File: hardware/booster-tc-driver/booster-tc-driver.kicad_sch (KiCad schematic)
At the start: 52 parts, among them J1 62201021121, J2 EHT-105-01-S-D, Q1 T2N7002AK, U1 STM32F405RGTx, U2 LT1963AxST-3.3, U3 MAX9202ESD+, U4 IF-D95T << must be T, U6 IF-D95T << must be T, U7 TC7662Bx0A

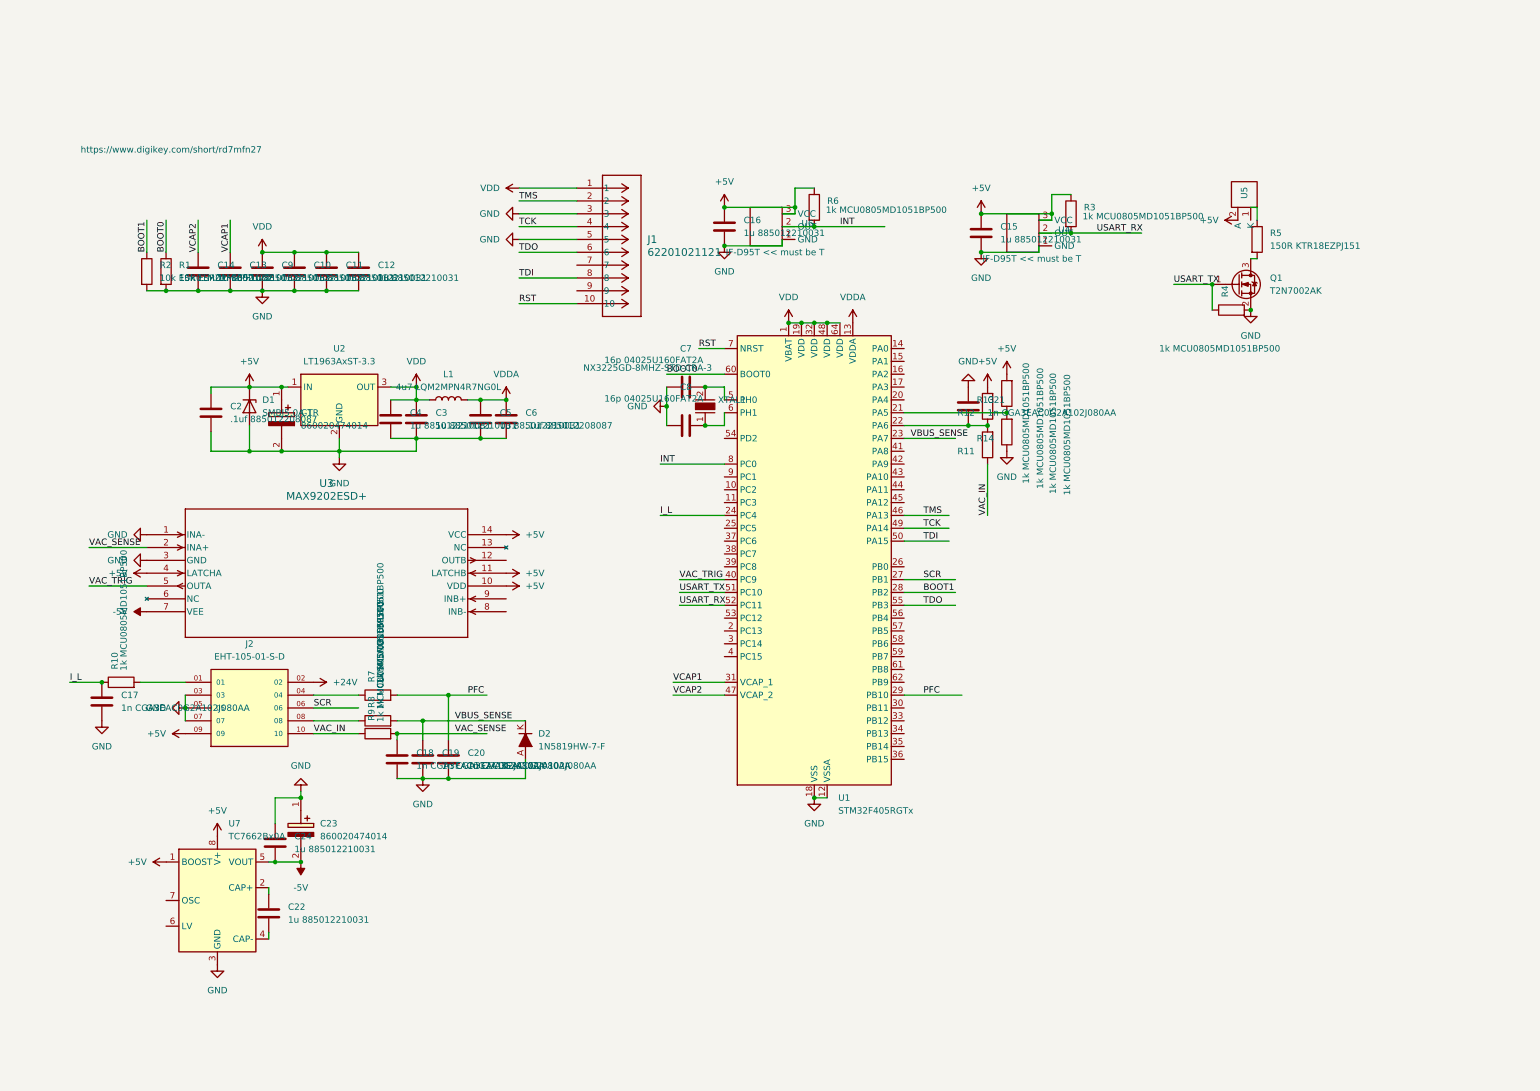
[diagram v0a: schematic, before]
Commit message: pin assignments
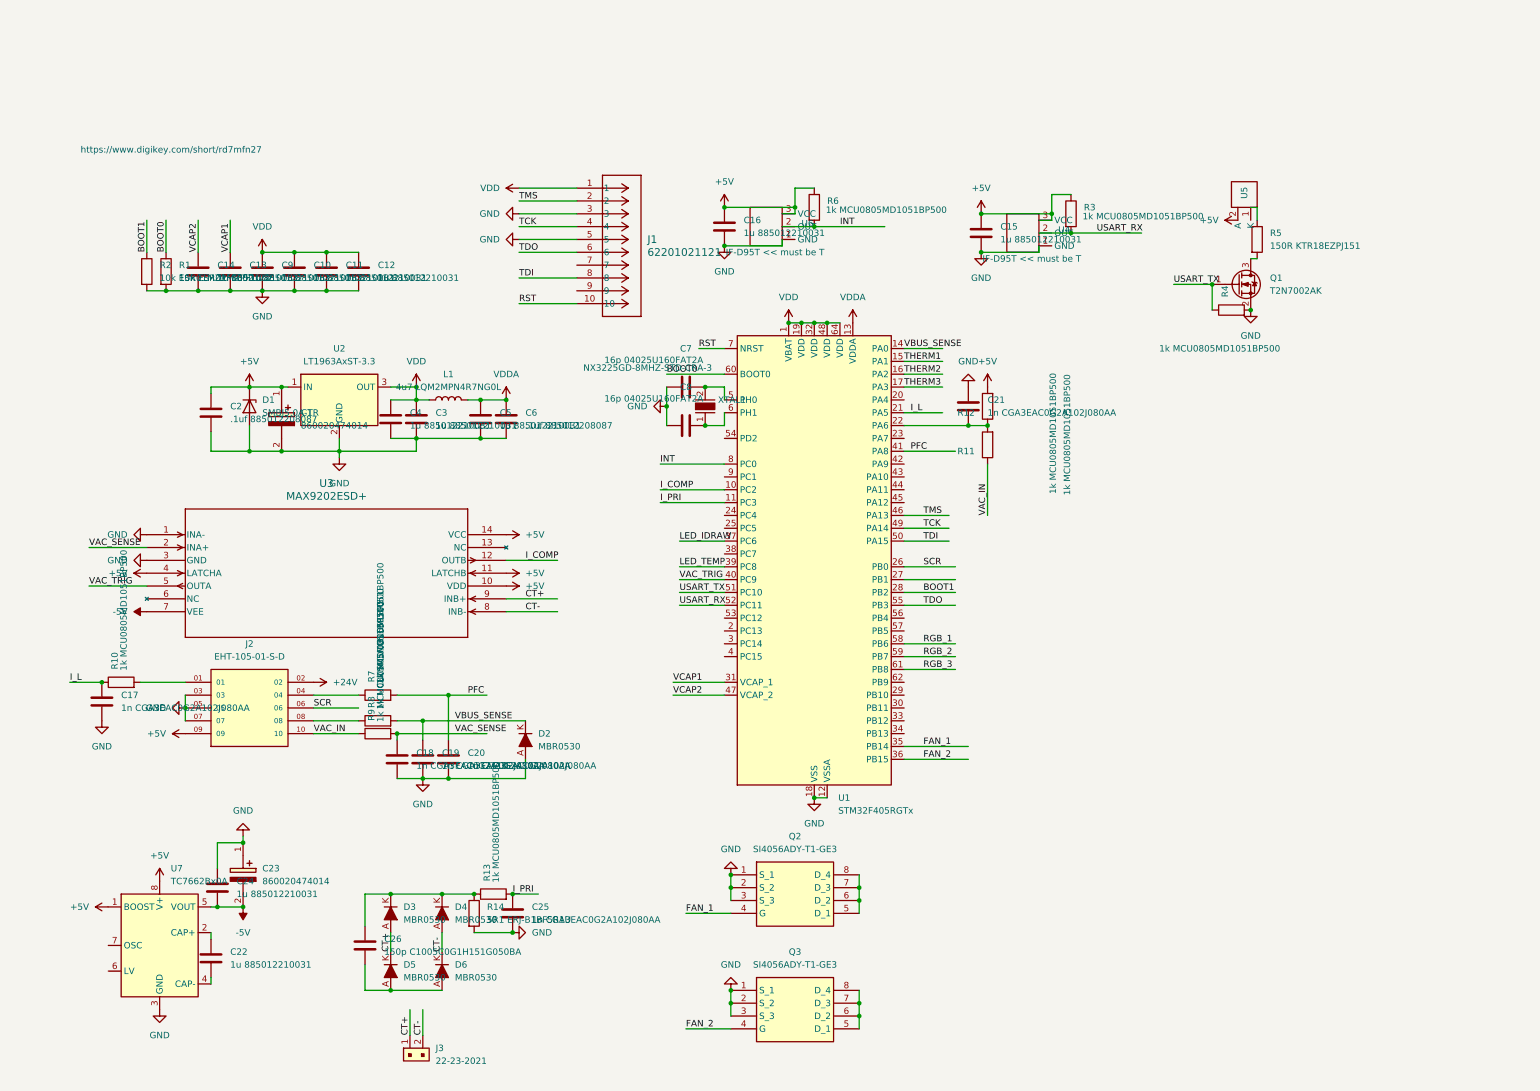
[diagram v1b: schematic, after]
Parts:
- added C25: 1n CGA3EAC0G2A102J080AA, Capacitor_SMD:C_0603_1608Metric_Pad1.08x0.95mm_HandSolder, symbol Device:C
- added C26: 150p C1005C0G1H151G050BA, Capacitor_SMD:C_01005_0402Metric_Pad0.57x0.30mm_HandSolder, symbol Device:C
- added D3, D4, D5, D6: MBR0530, digikey-footprints:SOD-123, symbol dk_Diodes-Rectifiers-Single:1N5819HW-7-F
- added J3: 22-23-2021, digikey-footprints:PinHeader_1x2_P2.54mm_Drill1.02mm, symbol dk_Rectangular-Connectors-Headers-Male-Pins:22-23-2021
- added Q2, Q3: SI4056ADY-T1-GE3, Library:SOIC127P600X175-8N, symbol SI4056ADY-T1-GE3:SI4056ADY-T1-GE3
- D2: value 1N5819HW-7-F -> MBR0530
- R14: value 1k MCU0805MD1051BP500 -> 5R1 ERJ-B1BF5R1U; footprint Resistor_SMD:R_0805_2012Metric_Pad1.20x1.40mm_HandSolder -> Resistor_SMD:R_1020_2550Metric_Pad1.33x5.20mm_HandSolder
- U3: footprint 21-0041B_14 -> Library:21-0041B_14-L
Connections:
- net +5V: no longer R13.2
- net GND: now also R14.2, C25.2, Q2.1 (S_1), Q2.2 (S_2), Q2.3 (S_3), Q3.1 (S_1), Q3.2 (S_2), Q3.3 (S_3); no longer R14.1
- net I_L: now also U1.21 (PA5); no longer U1.24 (PC4)
- net PFC: now also U1.41 (PA8); no longer U1.29 (PB10)
- net SCR: now also U1.26 (PB0); no longer U1.27 (PB1)
- net VBUS_SENSE: now also U1.14 (PA0); no longer U1.23 (PA7)
- net I_COMP: now reaches U1.10 (PC2)
- net I_COMP: now also U3.12 (OUTB)
- net I_PRI: now reaches U1.11 (PC3)
- net I_PRI: now also R13.2, C25.1
- net THERM1: now reaches U1.15 (PA1)
- net THERM2: now reaches U1.16 (PA2)
- net THERM3: now reaches U1.17 (PA3)
- net FAN_1: now reaches U1.35 (PB14)
- net FAN_1: now also Q2.4 (G)
- net FAN_2: now reaches U1.36 (PB15)
- net FAN_2: now also Q3.4 (G)
- net LED_IDRAW: now reaches U1.37 (PC6)
- net LED_TEMP: now reaches U1.39 (PC8)
- net RGB_1: now reaches U1.58 (PB6)
- net RGB_2: now reaches U1.59 (PB7)
- net RGB_3: now reaches U1.61 (PB8)
- net CT-: now reaches U3.8 (INB-)
- net CT-: now also D4.A, D6.K, J3.2
- net CT+: now reaches U3.9 (INB+)
- net CT+: now also D3.A, D5.K, J3.1
- new net: C26.1, D3.K, D4.K, R13.1, R14.1
- new net: C26.2, D5.A, D6.A
- new net: Q2.5 (D_1), Q2.6 (D_2), Q2.7 (D_3), Q2.8 (D_4)
- new net: Q3.5 (D_1), Q3.6 (D_2), Q3.7 (D_3), Q3.8 (D_4)
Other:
- moved on the sheet: C22, C23, C24, U7

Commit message: driver pcb
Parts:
- removed C1, C23: 860020474014, Library:CAPPRD350W52D800H1300, symbol New_Library:860020474014
- removed C14, C3, C4: 1u 885012210031, Capacitor_SMD:C_1812_4532Metric_Pad1.57x3.40mm_HandSolder, symbol Device:C
- removed C18, C21: 1n CGA3EAC0G2A102J080AA, Capacitor_SMD:C_0603_1608Metric_Pad1.08x0.95mm_HandSolder, symbol Device:C
- removed C26: 150p C1005C0G1H151G050BA, Capacitor_SMD:C_01005_0402Metric_Pad0.57x0.30mm_HandSolder, symbol Device:C
- removed J3: 22-23-2021, digikey-footprints:PinHeader_1x2_P2.54mm_Drill1.02mm, symbol dk_Rectangular-Connectors-Headers-Male-Pins:22-23-2021
- removed L1: 4u7 LQM2MPN4R7NG0L, Inductor_SMD:L_Murata_DFE201610P, symbol Device:L
- removed Q2, Q3: SI4056ADY-T1-GE3, Library:SOIC127P600X175-8N, symbol SI4056ADY-T1-GE3:SI4056ADY-T1-GE3
- removed U1: STM32F405RGTx, Package_QFP:LQFP-64_10x10mm_P0.5mm, symbol MCU_ST_STM32F4:STM32F405RGTx
- removed U2: LT1963AxST-3.3, Package_TO_SOT_SMD:SOT-223-3_TabPin2, symbol Regulator_Linear:LT1963AxST-3.3
- removed U3: MAX9202ESD+, Library:21-0041B_14-L, symbol 2024-07-01_19-30-11:MAX9202ESD+
- removed U7: TC7662Bx0A, Package_SO:SOIC-8_3.9x4.9mm_P1.27mm, symbol Converter_DCDC:TC7662Bx0A
- removed XTAL1: NX3225GD-8MHZ-STD-CRA-3, digikey-footprints:SMD-2_3.2x2.5mm, symbol dk_Crystals:NX3225GD-8MHZ-STD-CRA-3
- added C1, C31, C37: 1n CGA3EAC0G2A102J080AA, Capacitor_SMD:C_0603_1608Metric_Pad1.08x0.95mm_HandSolder, symbol Device:C
- added C21, C3, C43, C45: 330u 860020575013, Library:860020575013, symbol Device:C_Polarized
- added C23, C27, C28, C32, C33, C35, C36, C40, C41, C42, C51, C52: .1uf 885012208087, Capacitor_SMD:C_1206_3216Metric_Pad1.33x1.80mm_HandSolder, symbol Device:C
- added C29, C34, C46, C47, C48, C49: 2u2 C3225X7R1H225K250AB, Capacitor_SMD:C_1210_3225Metric_Pad1.33x2.70mm_HandSolder, symbol Device:C
- added C30, C39: 22n VJ0805Y223KBBBE31, Capacitor_SMD:C_0805_2012Metric_Pad1.18x1.45mm_HandSolder, symbol Device:C
- added C38, C50: .1uf C0603C104K3RECTU, Capacitor_SMD:C_0603_1608Metric_Pad1.08x0.95mm_HandSolder, symbol Device:C
- added D10, D7, D8, D9: MBR0530, digikey-footprints:SOD-123, symbol dk_Diodes-Rectifiers-Single:1N5819HW-7-F
- added D13: SMBJ5.0A-TR, kicad-libraries-master:DO-214AA, symbol Device:D_Zener
- added D14, D15: PMEG4050EP, Diode_SMD:D_SOD-128, symbol Diode:PMEG4050EP
- added D16: 5700100132F, Library:LED_5700100132F, symbol 5700100132F:5700100132F
- added IC1, IC2: AD5160BRJZ5-RL7, Library:SOT65P280X145-8N, symbol New_Library:AD5160BRJZ5-RL7
- added IC3: BD50FD0WHFP-TR, Library:BD50FD0WHFPTR, symbol New_Library:BD50FD0WHFP-TR
- added IC4: CAT4109V-GT2, Library:CAT4109V-GT2, symbol New_Library:CAT4109V-GT2
- added IC5: L4940D2T12-TR, Library:L4940D2T12-TR, symbol New_Library:L4940D2T12-TR
- added J10, J3, J7: 3-647166-2, Library:36471662, symbol New_Library:3-647166-2
- added J6: 22-23-2021, digikey-footprints:PinHeader_1x2_P2.54mm_Drill1.02mm, symbol dk_Rectangular-Connectors-Headers-Male-Pins:22-23-2021
- added J8: B4B-PH-SM4-TB, Library:CONN_B4B-PH-SM4-TB_JST, symbol New_Library:B4B-PH-SM4-TB
- added L2: 4u7 LQM2MPN4R7NG0L, Inductor_SMD:L_Murata_DFE201610P, symbol Device:L
- added L4, L5: 22u 7443551221, Library:7443551221, symbol Device:L
- added R15: 47k CRCW080547K0FKEA, Resistor_SMD:R_0805_2012Metric_Pad1.20x1.40mm_HandSolder, symbol Device:R
- added R16: 470k CRCW0805470KFKTA, Resistor_SMD:R_0805_2012Metric_Pad1.20x1.40mm_HandSolder, symbol Device:R
- added R17: 3k CRCW08053K00FKTA, Resistor_SMD:R_0805_2012Metric_Pad1.20x1.40mm_HandSolder, symbol Device:R
- added R18: 82k CRCW080582K0FKEA, Resistor_SMD:R_0805_2012Metric_Pad1.20x1.40mm_HandSolder, symbol Device:R
- added R21: 1k MCU0805MD1051BP500, Resistor_SMD:R_0805_2012Metric_Pad1.20x1.40mm_HandSolder, symbol Device:R
- added R25, R26, R27: 24k9 CRCW060324K9FKEA, Resistor_SMD:R_0603_1608Metric_Pad0.98x0.95mm_HandSolder, symbol Device:R
- added R33, R34: 10k CRCW080510K0DHEAP, Resistor_SMD:R_0805_2012Metric_Pad1.20x1.40mm_HandSolder, symbol Device:R
- added SW1: SW_SPDT, Library:B12JV, symbol Switch:SW_SPDT
- added U1: STM32G474CBTx, Package_QFP:LQFP-48_7x7mm_P0.5mm, symbol MCU_ST_STM32G4:STM32G474CBTx
- added U10: LT1963AxST-3.3, Package_TO_SOT_SMD:SOT-223-3_TabPin2, symbol Regulator_Linear:LT1963AxST-3.3
- added U2, U7: AOZ1284PI, Package_SO:SOIC-8-1EP_3.9x4.9mm_P1.27mm_EP2.29x3mm, symbol New_Library:AOZ1284PI
- added U3: CSTNE8M00G550000R0, Library:CSTNE16M0V530000R0, symbol New_Library:CSTNE8M00G550000R0
- C10, C11, C12, C13, C9: value 1u 885012210031 -> .1uf C0603C104K3RECTU; footprint Capacitor_SMD:C_1812_4532Metric_Pad1.57x3.40mm_HandSolder -> Capacitor_SMD:C_0603_1608Metric_Pad1.08x0.95mm_HandSolder
- C15, C16, C5: value 1u 885012210031 -> 2u2 C3225X7R1H225K250AB; footprint Capacitor_SMD:C_1812_4532Metric_Pad1.57x3.40mm_HandSolder -> Capacitor_SMD:C_1210_3225Metric_Pad1.33x2.70mm_HandSolder
- C2: value .1uf 885012208087 -> 2u2 C3225X7R1H225K250AB; footprint Capacitor_SMD:C_1206_3216Metric_Pad1.33x1.80mm_HandSolder -> Capacitor_SMD:C_1210_3225Metric_Pad1.33x2.70mm_HandSolder
- C20: value 1n CGA3EAC0G2A102J080AA -> 2u2 C3225X7R1H225K250AB; footprint Capacitor_SMD:C_0603_1608Metric_Pad1.08x0.95mm_HandSolder -> Capacitor_SMD:C_1210_3225Metric_Pad1.33x2.70mm_HandSolder
- C22, C24: value 1u 885012210031 -> .1uf 885012208087; footprint Capacitor_SMD:C_1812_4532Metric_Pad1.57x3.40mm_HandSolder -> Capacitor_SMD:C_1206_3216Metric_Pad1.33x1.80mm_HandSolder
- C7: value 16p 04025U160FAT2A -> 1n CGA3EAC0G2A102J080AA; footprint Capacitor_SMD:C_0402_1005Metric_Pad0.74x0.62mm_HandSolder -> Capacitor_SMD:C_0603_1608Metric_Pad1.08x0.95mm_HandSolder
- C8: value 16p 04025U160FAT2A -> 1u C1206C105K5RACTU; footprint Capacitor_SMD:C_0402_1005Metric_Pad0.74x0.62mm_HandSolder -> Capacitor_SMD:C_1206_3216Metric_Pad1.33x1.80mm_HandSolder
- D1: value SMBJ5.0A-TR -> SMBJ3V3
- D2: MPN 1N5819HW-7-F -> MBR0530
- D3, D4, D5, D6: value MBR0530 -> 1N5819HW-7-F
- R1: value 10k ESR01MZPF1002 -> 3k CRCW08053K00FKTA; footprint Resistor_SMD:R_0402_1005Metric_Pad0.72x0.64mm_HandSolder -> Resistor_SMD:R_0805_2012Metric_Pad1.20x1.40mm_HandSolder
- R11: value 1k MCU0805MD1051BP500 -> 47k CRCW080547K0FKEA
- R12: value 1k MCU0805MD1051BP500 -> 470k CRCW0805470KFKTA
- R2: value 10k ESR01MZPF1002 -> 82k CRCW080582K0FKEA; footprint Resistor_SMD:R_0402_1005Metric_Pad0.72x0.64mm_HandSolder -> Resistor_SMD:R_0805_2012Metric_Pad1.20x1.40mm_HandSolder
- U5: value ~ -> IF-E96E
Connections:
- net -5V is gone; now on net +24V: C24.2
- net VCAP1 is gone; now on net THERM2: C13.1
- net +24V: now also C21.1, C27.2, C36.2, C52.2, IC3.1 (CTL), IC3.2 (VCC), IC5.1 (INPUT), J6.2, U2.9 (VIN), U7.9 (VIN)
- net +5V: now also C20.1, C22.2, C5.1, C6.1, U5.2 (A), C40.2, C46.1, D13.1 (K), D16.1, D16.3, D16.5, IC1.2 (VDD), IC2.2 (VDD), IC3.4 (VO), U10.1 (IN), U7.8 (EN); no longer D1.1 (K), R12.2
- net CT+: now also D4.A, D6.K, J3.2; no longer D3.A, D5.K
- net CT-: now also D3.A, D5.K, J3.1; no longer D4.A, D6.K
- net GND: now also C10.1, C22.1, C7.2, D5.A, D6.A, R11.1, C1.2, C21.2, C27.1, C28.2, C29.1, C3.2, C30.2, C31.1, C32.2, C33.2, C34.2, C35.2, C36.1, C37.1, C38.1, C39.2, C40.1, C41.2, C43.2, C45.2, C46.2, C47.1, C48.2, C49.2, C50.2, C51.2, C52.1, D13.2 (A), D14.2 (A), D15.2 (A), D9.A, IC1.1 (W), IC1.3 (GND), IC1.7 (B), IC2.1 (W), IC2.3 (GND), IC2.7 (B), IC3.3 (GND_1), IC3.5 (ADJ), IC3.6 (GND_2), IC4.1 (PGND), IC4.2 (GND), IC5.4 (GND), J10.2, J6.1, J7.2, J8.1, J8.3, R15.1, R25.1, R26.1, R27.1, SW1.1 (A), U1.19 (VSSA), U1.23 (VSS), U1.35 (VSS), U1.47 (VSS), U10.2 (GND), U2.3 (GND), U3.2 (GND), U7.3 (GND); no longer C10.2, C7.1, R1.2, R2.2
- net I_L: now also D8.A
- net PFC: now also J2.04; no longer C20.1, R7.2
- net RST: now also U1.7 (PG10)
- net TCK: now also U1.38 (PA14)
- net TDI: now also U1.39 (PA15)
- net TDO: now also U1.40 (PB3)
- net THERM1: now also C38.2, J8.2, R34.1
- net THERM2: now also J8.4, R33.1
- net TMS: now also U1.37 (PA13)
- net VAC_IN: now also R7.2; no longer R11.1, R9.1
- net VAC_SENSE: now also C7.1, R7.1, D10.A, D9.K
- net VBUS_SENSE: now also D7.A
- net VDD: now also D1.1 (K), C3.1, C32.1, C33.1, D10.K, D7.K, D8.K, IC4.15 (OE), IC4.16 (VDD), L2.1, SW1.3 (C), U1.1 (VBAT), U1.24 (VDD), U1.36 (VDD), U1.48 (VDD), U10.3 (OUT); no longer C10.1
- net VDDA: now also C34.1, C35.1, C50.1, L2.2, U1.21 (VDDA); no longer C5.1, C6.1
- net VBUS_IN: now reaches J2.08, R8.1
- net at D3.K, D4.K, R13.1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: now also C1.1
- net at R12.1: now also C31.2; no longer R11.2
- net VREF: now reaches C8.2
- net VREF: now also C10.2, R9.1, R33.2, R34.2, U1.20 (VREF+)
- net I_L_IN: now reaches J2.01, R10.2
- net BOOT0: no longer names the net of R1.1
- net BOOT0: now also IC1.8 (A)
- net BOOT1 renamed VFAN_OUT
- net VFAN_OUT: now also C29.2, C47.2, C48.1, C49.1, J7.1, L4.2
- new net: IC2.8 (A), R17.1
- new net: C41.1, R17.2, R18.2, U7.6 (FB)
- new net: R21.1, SW1.2 (B)
- new net: R12.2, U2.5 (COMP)
- new net: U1.5 (PF0), U3.3 (OUTPUT)
- new net: U1.6 (PF1), U3.1 (INPUT)
- new net: R15.2, U7.4 (FSW)
- new net: D16.4, IC4.10 (LED2)
- new net: D16.2, IC4.11 (LED1)
- new net: IC4.6 (RSET3), R25.2
- new net: IC4.7 (RSET2), R26.2
- new net: IC4.8 (RSET1), R27.2
- new net: D16.6, IC4.9 (LED3)
- new net: C42.1, U7.2 (BST)
- new net: C42.2, D15.1 (K), L5.1, U7.1 (LX)
- new net: C37.2, R16.1
- new net: R16.2, U7.5 (COMP)
- new net: C28.1, R1.2, R2.2, U2.6 (FB)
- new net: C23.1, U2.2 (BST)
- new net: C23.2, D14.1 (K), L4.1, U2.1 (LX)
- new net: C39.1, U7.7 (SS)
- new net: C30.1, U2.7 (SS)
- new net: R11.2, U2.4 (FSW)
- new net +12V: C45.1, C51.1, IC5.3 (OUTPUT), J10.1
- new net CS_DRIVE: IC2.6 (~{CS})
- new net CS_FAN: IC1.6 (~{CS})
- new net FAN_EN: U2.8 (EN)
- new net LED_I_IN: IC4.5 (PWM1)
- new net LED_TMP: IC4.4 (PWM2)
- new net LED_VBUS: IC4.3 (PWM3)
- new net MODE_IN: R21.2
- new net SPI_CLK: IC1.4 (CLK), IC2.4 (CLK)
- new net SPI_MOSI: IC1.5 (SDI), IC2.5 (SDI)
- new net VDRIVE: C43.1, L5.2, R18.1
- no-connect marks 0 -> 1
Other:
- added sheet Gate Drive Out (booster-tc-driver-gatedrive.kicad_sch)
- note added: "https://www.digikey.com/short/rd7mfn27 https://www.digikey.com/en/products/detail/bud-industries/exn-23351-bl/5886290"
- note removed: "https://www.digikey.com/short/rd7mfn27"
- moved on the sheet: C17, C19, C25, D2, D3, D4, D5, D6, J1, J2, Q1, R10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
